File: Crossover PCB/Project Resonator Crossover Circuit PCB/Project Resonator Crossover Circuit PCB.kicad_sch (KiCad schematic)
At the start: 21 parts

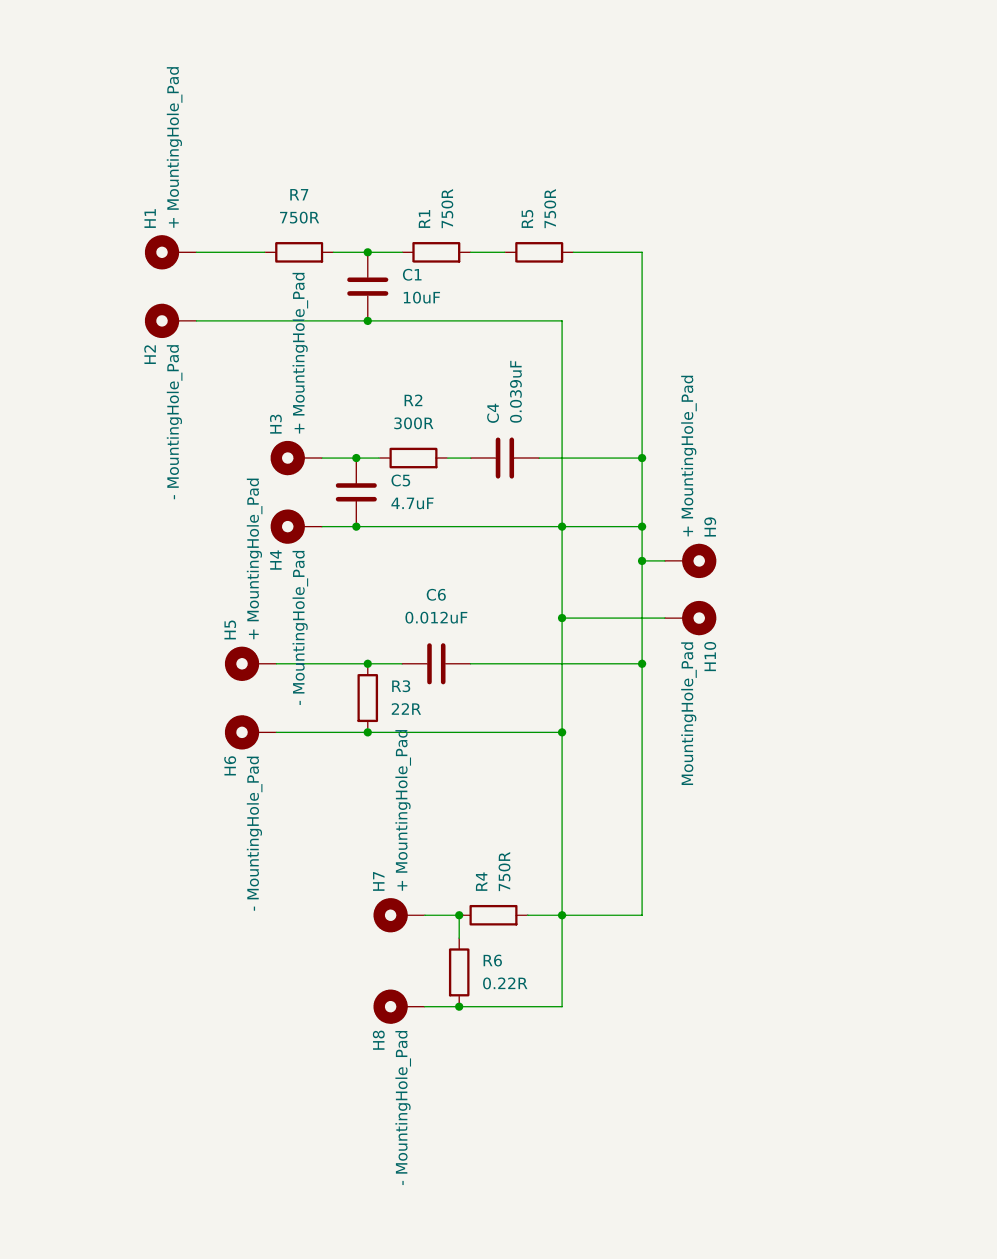
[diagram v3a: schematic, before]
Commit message: Redesigned Layout of PCB to Wrap Shell, Updated Overall Shell Design, Removed Bluetooth Code experimental, Rendered New colorways mockups
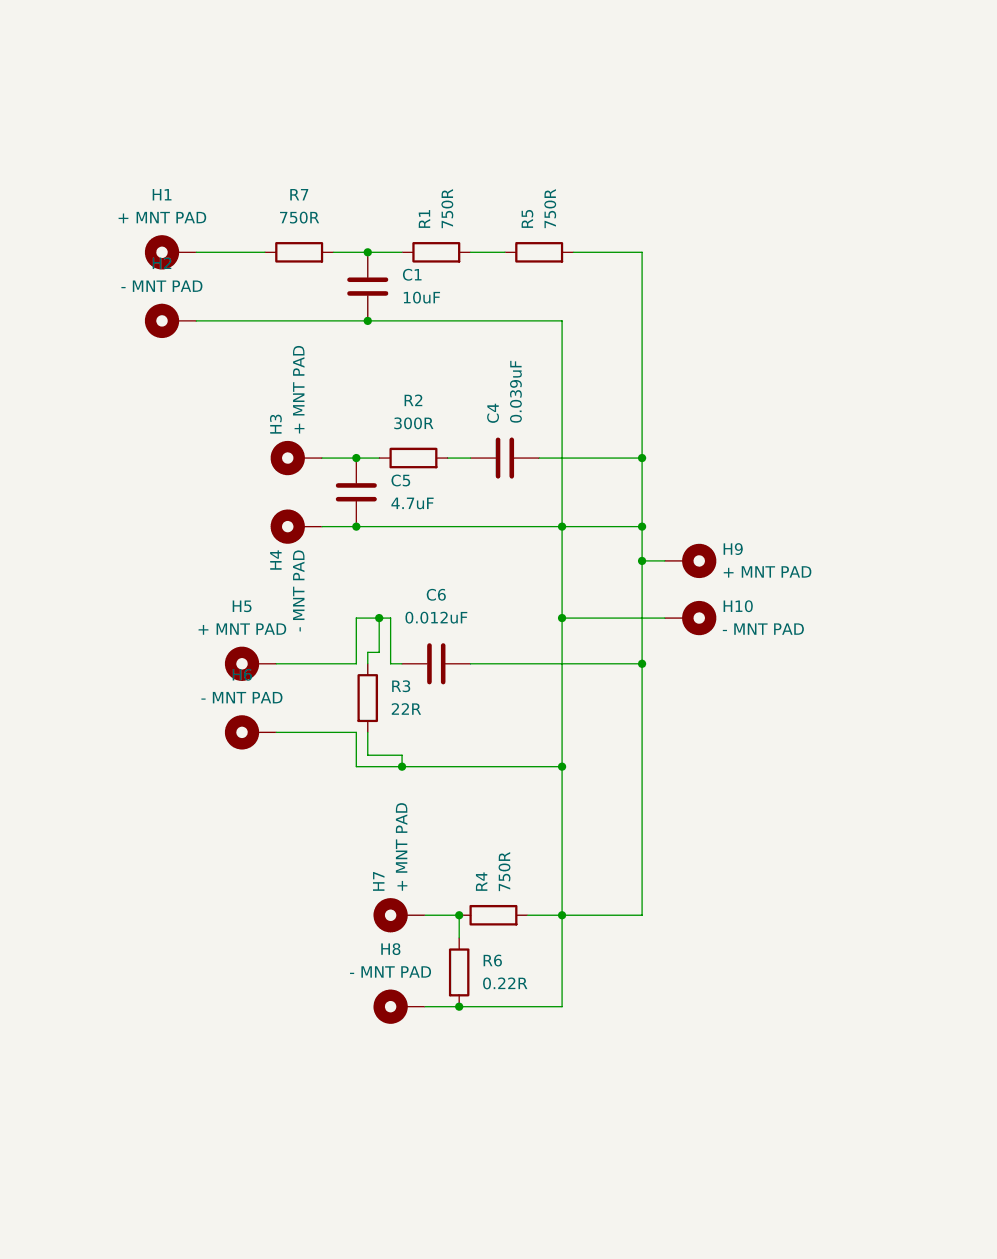
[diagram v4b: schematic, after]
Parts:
- H1, H3, H5, H7, H9: value + MountingHole_Pad -> + MNT PAD
- H10: value MountingHole_Pad -> - MNT PAD
- H2, H4, H6, H8: value - MountingHole_Pad -> - MNT PAD
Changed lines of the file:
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@@
 	)
 	(junction
-		(at 144.78 106.68)
+		(at 148.59 110.49)
 		(diameter 0)
 		(color 0 0 0 0)
@@
 	)
 	(junction
-		(at 166.37 106.68)
+		(at 166.37 110.49)
 		(diameter 0)
 		(color 0 0 0 0)
@@
 	)
 	(junction
-		(at 144.78 99.06)
+		(at 146.05 93.98)
 		(diameter 0)
 		(color 0 0 0 0)
@@
 	(wire
 		(pts
+			(xy 143.51 93.98) (xy 143.51 99.06)
+		)
+		(stroke
+			(width 0)
+			(type default)
+		)
+	)
+	(wire
+		(pts
 			(xy 154.94 127) (xy 154.94 129.54)
 		)
@@
 	(wire
 		(pts
-			(xy 134.62 99.06) (xy 144.78 99.06)
-		)
-		(stroke
-			(width 0)
-			(type default)
-		)
-	)
-	(wire
-		(pts
-			(xy 144.78 99.06) (xy 148.59 99.06)
+			(xy 148.59 109.22) (xy 144.78 109.22)
+		)
+		(stroke
+			(width 0)
+			(type default)
+		)
+	)
+	(wire
+		(pts
+			(xy 143.51 93.98) (xy 146.05 93.98)
+		)
+		(stroke
+			(width 0)
+			(type default)
+		)
+	)
+	(wire
+		(pts
+			(xy 146.05 93.98) (xy 147.32 93.98)
 		)
 		(stroke
@@
 	(wire
 		(pts
+			(xy 143.51 106.68) (xy 134.62 106.68)
+		)
+		(stroke
+			(width 0)
+			(type default)
+		)
+	)
+	(wire
+		(pts
 			(xy 175.26 87.63) (xy 177.8 87.63)
 		)
@@
 	(wire
 		(pts
+			(xy 144.78 97.79) (xy 144.78 99.06)
+		)
+		(stroke
+			(width 0)
+			(type default)
+		)
+	)
+	(wire
+		(pts
+			(xy 146.05 97.79) (xy 144.78 97.79)
+		)
+		(stroke
+			(width 0)
+			(type default)
+		)
+	)
+	(wire
+		(pts
+			(xy 146.05 93.98) (xy 146.05 97.79)
+		)
+		(stroke
+			(width 0)
+			(type default)
+		)
+	)
+	(wire
+		(pts
+			(xy 166.37 110.49) (xy 166.37 127)
+		)
+		(stroke
+			(width 0)
+			(type default)
+		)
+	)
+	(wire
+		(pts
 			(xy 151.13 137.16) (xy 154.94 137.16)
 		)
@@
 	(wire
 		(pts
+			(xy 144.78 109.22) (xy 144.78 106.68)
+		)
+		(stroke
+			(width 0)
+			(type default)
+		)
+	)
+	(wire
+		(pts
 			(xy 143.51 83.82) (xy 166.37 83.82)
 		)
@@
 	(wire
 		(pts
-			(xy 166.37 93.98) (xy 166.37 106.68)
-		)
-		(stroke
-			(width 0)
-			(type default)
-		)
-	)
-	(wire
-		(pts
 			(xy 175.26 87.63) (xy 175.26 99.06)
 		)
@@
 	(wire
 		(pts
-			(xy 166.37 106.68) (xy 166.37 127)
+			(xy 147.32 93.98) (xy 147.32 99.06)
+		)
+		(stroke
+			(width 0)
+			(type default)
+		)
+	)
+	(wire
+		(pts
+			(xy 166.37 93.98) (xy 166.37 110.49)
 		)
 		(stroke
@@
 	(wire
 		(pts
+			(xy 143.51 99.06) (xy 134.62 99.06)
+		)
+		(stroke
+			(width 0)
+			(type default)
+		)
+	)
+	(wire
+		(pts
+			(xy 148.59 110.49) (xy 148.59 109.22)
+		)
+		(stroke
+			(width 0)
+			(type default)
+		)
+	)
+	(wire
+		(pts
+			(xy 147.32 99.06) (xy 148.59 99.06)
+		)
+		(stroke
+			(width 0)
+			(type default)
+		)
+	)
+	(wire
+		(pts
 			(xy 144.78 53.34) (xy 148.59 53.34)
 		)
@@
 	(wire
 		(pts
-			(xy 144.78 106.68) (xy 166.37 106.68)
+			(xy 148.59 110.49) (xy 166.37 110.49)
 		)
 		(stroke
@@
 	(wire
 		(pts
-			(xy 134.62 106.68) (xy 144.78 106.68)
+			(xy 143.51 110.49) (xy 143.51 106.68)
+		)
+		(stroke
+			(width 0)
+			(type default)
+		)
+	)
+	(wire
+		(pts
+			(xy 143.51 110.49) (xy 148.59 110.49)
 		)
 		(stroke
@@
 		(fields_autoplaced yes)
 		(property "Reference" "H8"
-			(at 146.0499 139.7 0)
-			(effects
-				(font
-					(size 1.27 1.27)
-				)
-				(justify left)
-			)
-		)
-		(property "Value" "-  MountingHole_Pad"
-			(at 148.5899 139.7 0)
-			(effects
-				(font
-					(size 1.27 1.27)
-				)
-				(justify left)
+			(at 147.32 130.81 90)
+			(effects
+				(font
+					(size 1.27 1.27)
+				)
+			)
+		)
+		(property "Value" "-  MNT PAD"
+			(at 147.32 133.35 90)
+			(effects
+				(font
+					(size 1.27 1.27)
+				)
 			)
 		)
@@
 			)
 		)
-		(property "Value" "+ MountingHole_Pad"
+		(property "Value" "+ MNT PAD"
 			(at 137.1599 73.66 0)
 			(effects
@@
 		(fields_autoplaced yes)
 		(property "Reference" "H9"
-			(at 182.8801 85.09 0)
-			(effects
-				(font
-					(size 1.27 1.27)
-				)
-				(justify left)
-			)
-		)
-		(property "Value" "+ MountingHole_Pad"
-			(at 180.3401 85.09 0)
+			(at 184.15 86.3599 90)
+			(effects
+				(font
+					(size 1.27 1.27)
+				)
+				(justify left)
+			)
+		)
+		(property "Value" "+ MNT PAD"
+			(at 184.15 88.8999 90)
 			(effects
 				(font
@@
 		(fields_autoplaced yes)
 		(property "Reference" "H5"
-			(at 129.5399 96.52 0)
-			(effects
-				(font
-					(size 1.27 1.27)
-				)
-				(justify left)
-			)
-		)
-		(property "Value" "+ MountingHole_Pad"
-			(at 132.0799 96.52 0)
-			(effects
-				(font
-					(size 1.27 1.27)
-				)
-				(justify left)
+			(at 130.81 92.71 90)
+			(effects
+				(font
+					(size 1.27 1.27)
+				)
+			)
+		)
+		(property "Value" "+ MNT PAD"
+			(at 130.81 95.25 90)
+			(effects
+				(font
+					(size 1.27 1.27)
+				)
 			)
 		)
@@
 		(fields_autoplaced yes)
 		(property "Reference" "H10"
-			(at 182.8801 96.52 0)
-			(effects
-				(font
-					(size 1.27 1.27)
-				)
-				(justify left)
-			)
-		)
-		(property "Value" "MountingHole_Pad"
-			(at 180.3401 96.52 0)
+			(at 184.15 92.7099 90)
+			(effects
+				(font
+					(size 1.27 1.27)
+				)
+				(justify left)
+			)
+		)
+		(property "Value" "- MNT PAD"
+			(at 184.15 95.2499 90)
 			(effects
 				(font
@@
 			)
 		)
-		(property "Value" "+ MountingHole_Pad"
+		(property "Value" "+ MNT PAD"
 			(at 148.5899 124.46 0)
 			(effects
@@
 		(fields_autoplaced yes)
 		(property "Reference" "H1"
-			(at 120.6499 50.8 0)
-			(effects
-				(font
-					(size 1.27 1.27)
-				)
-				(justify left)
-			)
-		)
-		(property "Value" "+ MountingHole_Pad"
-			(at 123.1899 50.8 0)
-			(effects
-				(font
-					(size 1.27 1.27)
-				)
-				(justify left)
+			(at 121.92 46.99 90)
+			(effects
+				(font
+					(size 1.27 1.27)
+				)
+			)
+		)
+		(property "Value" "+ MNT PAD"
+			(at 121.92 49.53 90)
+			(effects
+				(font
+					(size 1.27 1.27)
+				)
 			)
 		)
@@
 		(fields_autoplaced yes)
 		(property "Reference" "H2"
-			(at 120.6499 63.5 0)
-			(effects
-				(font
-					(size 1.27 1.27)
-				)
-				(justify left)
-			)
-		)
-		(property "Value" "- MountingHole_Pad"
-			(at 123.1899 63.5 0)
-			(effects
-				(font
-					(size 1.27 1.27)
-				)
-				(justify left)
+			(at 121.92 54.61 90)
+			(effects
+				(font
+					(size 1.27 1.27)
+				)
+			)
+		)
+		(property "Value" "- MNT PAD"
+			(at 121.92 57.15 90)
+			(effects
+				(font
+					(size 1.27 1.27)
+				)
 			)
 		)
@@
 			)
 		)
-		(property "Value" "- MountingHole_Pad"
+		(property "Value" "- MNT PAD"
 			(at 137.1599 86.36 0)
 			(effects
@@
 		(fields_autoplaced yes)
 		(property "Reference" "H6"
-			(at 129.5399 109.22 0)
-			(effects
-				(font
-					(size 1.27 1.27)
-				)
-				(justify left)
-			)
-		)
-		(property "Value" "- MountingHole_Pad"
-			(at 132.0799 109.22 0)
-			(effects
-				(font
-					(size 1.27 1.27)
-				)
-				(justify left)
-			)
-		)
+			(at 130.81 100.33 90)
+			(effects
+				(font
+					(size 1.27 1.27)
+				)
+			)
+		)
+		(property "Value" "- MNT PAD"
+			(at 130.81 102.87 90)
+			(effects
+				(font
+					(size 1.27 1.27)
+				)
+			)
+		)

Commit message: updated PCB crossover to match the latest crossover diagram and fixed size to fit latest version of the shell
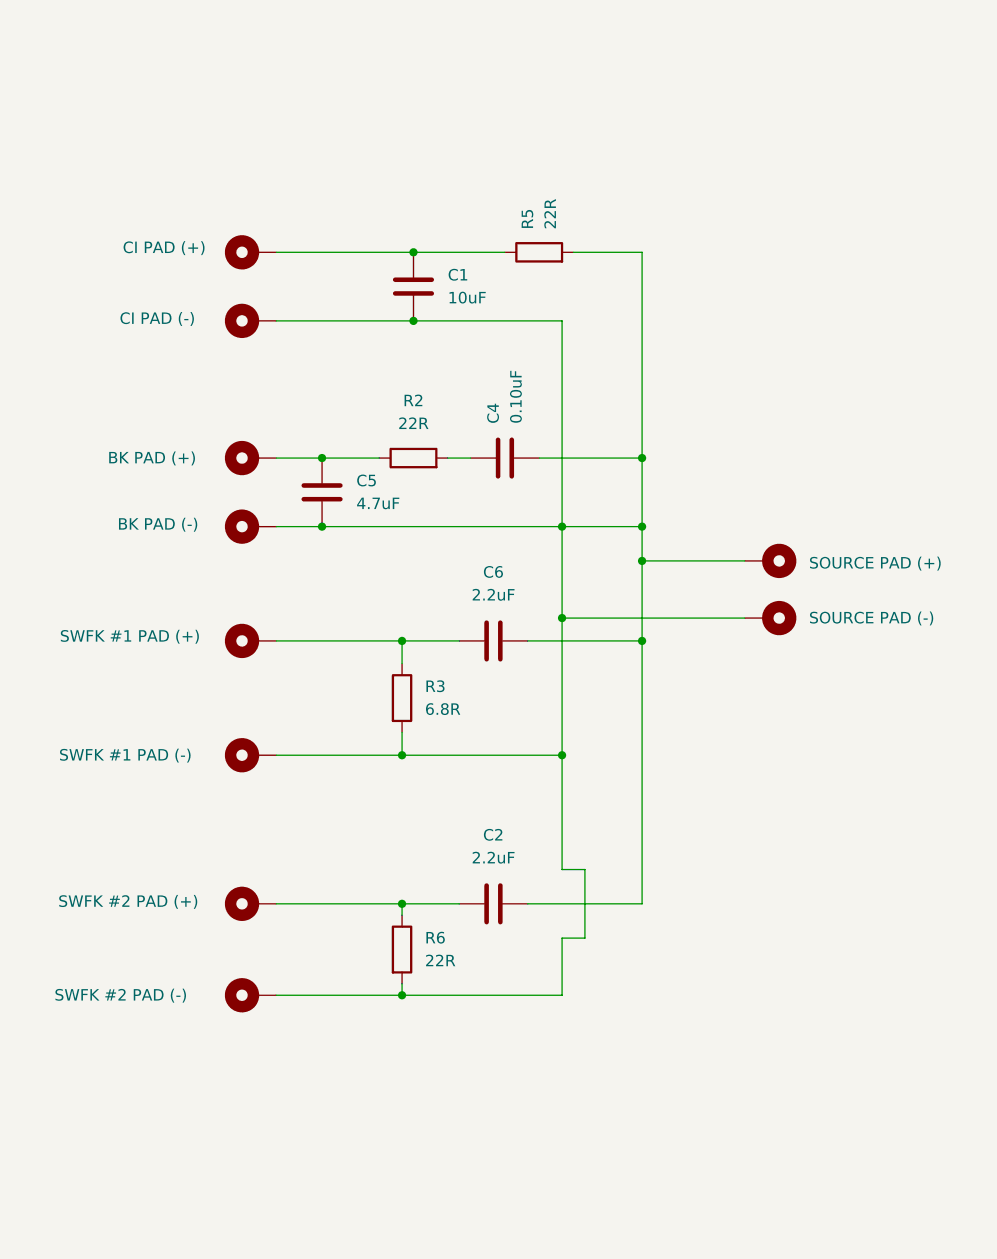
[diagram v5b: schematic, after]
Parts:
- removed R1, R4, R7: 750R, Resistor_SMD:R_0402_1005Metric_Pad0.72x0.64mm_HandSolder, symbol Device:R
- added C2: 2.2uF, Capacitor_SMD:C_0402_1005Metric_Pad0.74x0.62mm_HandSolder, symbol Device:C
- C4: value 0.039uF -> 0.10uF
- C6: value 0.012uF -> 2.2uF
- H1: value + MNT PAD -> CI PAD (+)
- H10: value - MNT PAD -> SOURCE PAD (-)
- H2: value - MNT PAD -> CI PAD (-); footprint TestPoint:TestPoint_Pad_1.0x1.0mm -> Connector:Conn_01x01_Pin
- H3: value + MNT PAD -> BK PAD (+)
- H4: value - MNT PAD -> BK PAD (-)
- H5: value + MNT PAD -> SWFK #1 PAD (+)
- H6: value - MNT PAD -> SWFK #1 PAD (-)
- H7: value + MNT PAD -> SWFK #2 PAD (+)
- H8: value - MNT PAD -> SWFK #2 PAD (-)
- H9: value + MNT PAD -> SOURCE PAD (+)
- R2: value 300R -> 22R
- R3: value 22R -> 6.8R
- R5: value 750R -> 22R
- R6: value 0.22R -> 22R
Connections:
- net at C1.2, C4.2, C5.2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: now also C2.2
- net at H7.1, R6.1: now also C2.1
- net at H1.1: now also C1.1, R5.1
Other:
- moved on the sheet: C1, C5, C6, R3, R6
